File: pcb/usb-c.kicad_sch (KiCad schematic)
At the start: 4 parts, among them J1 USB_C_Receptacle_PowerOnly_6P, J12 Conn_01x02_Pin

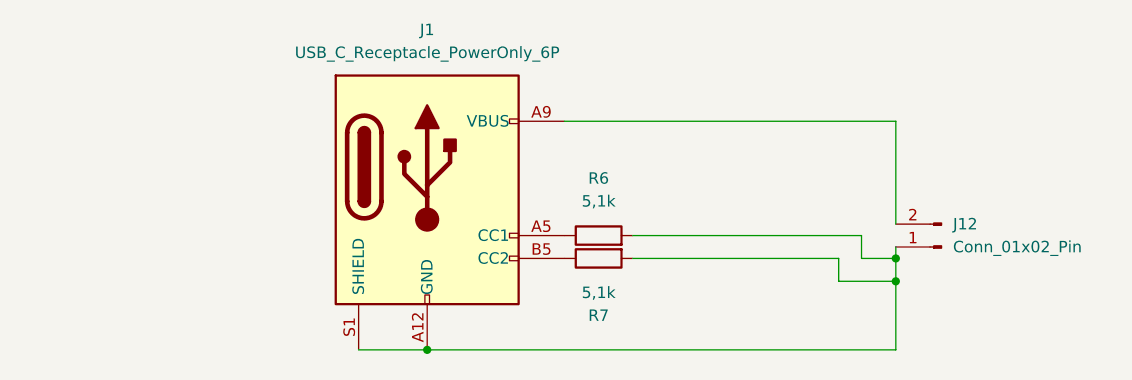
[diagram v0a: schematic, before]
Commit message: Finishing the usb-c module
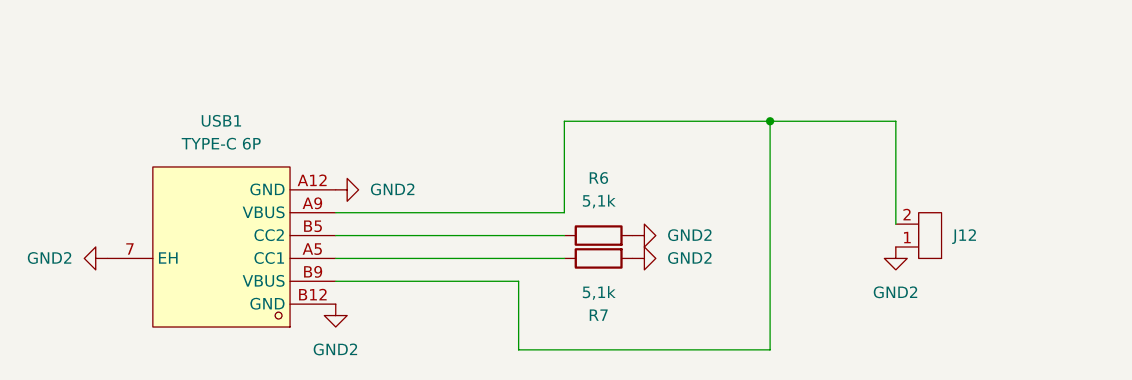
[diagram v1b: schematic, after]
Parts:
- removed J1: USB_C_Receptacle_PowerOnly_6P, Connector_USB:USB_C_Receptacle_GCT_USB4125-xx-x_6P_TopMnt_Horizontal, symbol Connector:USB_C_Receptacle_PowerOnly_6P
- removed J12: Conn_01x02_Pin, Library:copper_pad 2x, symbol Connector:Conn_01x02_Pin
- added J12: (no value), Library:copper_pad 2x, symbol New_Library:copper_pad_2x
- added USB1: TYPE-C 6P, lcsc_import:TYPE-C-SMD_TYPE-C-6P-073, symbol lcsc_import:TYPE-C6P
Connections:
- net GND2: now reaches R6.2, R7.2
- net GND2: now also J12.1, USB1.7 (EH), USB1.A12 (GND), USB1.B12 (GND)
- net at R6.1: now also USB1.B5 (CC2)
- net at R7.1: now also USB1.A5 (CC1)
- new net: J12.2, USB1.A9 (VBUS), USB1.B9 (VBUS)

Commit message: Finishing the carrier board with the new usb-c modul
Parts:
- renumbered R6 to R8, R7 to R9
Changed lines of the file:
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@@
 		(dnp no)
 		(fields_autoplaced yes)
-		(property "Reference" "#PWR037"
+		(property "Reference" "#PWR032"
 			(at 44.45 93.98 0)
 			(hide yes)
@@
 			(project "pcb"
 				(path "/2955ee96-3683-4cf6-bfa3-83b5e4980920/987d3c68-4f18-439b-bf60-3e9251430e23"
-					(reference "#PWR037")
+					(reference "#PWR032")
 					(unit 1)
 				)
@@
 		(dnp no)
 		(fields_autoplaced yes)
-		(property "Reference" "#PWR029"
+		(property "Reference" "#PWR037"
 			(at 138.43 99.06 0)
 			(hide yes)
@@
 			(project "pcb"
 				(path "/2955ee96-3683-4cf6-bfa3-83b5e4980920/987d3c68-4f18-439b-bf60-3e9251430e23"
-					(reference "#PWR029")
+					(reference "#PWR037")
 					(unit 1)
 				)
@@
 		(dnp no)
 		(fields_autoplaced yes)
-		(property "Reference" "#PWR034"
+		(property "Reference" "#PWR035"
 			(at 115.57 91.44 0)
 			(hide yes)
@@
 			(project "pcb"
 				(path "/2955ee96-3683-4cf6-bfa3-83b5e4980920/987d3c68-4f18-439b-bf60-3e9251430e23"
-					(reference "#PWR034")
+					(reference "#PWR035")
 					(unit 1)
 				)
@@
 		(dnp no)
 		(fields_autoplaced yes)
-		(property "Reference" "#PWR036"
+		(property "Reference" "#PWR034"
 			(at 76.2 105.41 0)
 			(hide yes)
@@
 			(project "pcb"
 				(path "/2955ee96-3683-4cf6-bfa3-83b5e4980920/987d3c68-4f18-439b-bf60-3e9251430e23"
-					(reference "#PWR036")
+					(reference "#PWR034")
 					(unit 1)
 				)
@@
 		(dnp no)
 		(fields_autoplaced yes)
-		(property "Reference" "#PWR035"
+		(property "Reference" "#PWR033"
 			(at 82.55 86.36 0)
 			(hide yes)
@@
 			(project "pcb"
 				(path "/2955ee96-3683-4cf6-bfa3-83b5e4980920/987d3c68-4f18-439b-bf60-3e9251430e23"
-					(reference "#PWR035")
+					(reference "#PWR033")
 					(unit 1)
 				)
@@
 		(dnp no)
 		(fields_autoplaced yes)
-		(property "Reference" "#PWR030"
+		(property "Reference" "#PWR036"
 			(at 115.57 93.98 0)
 			(hide yes)
@@
 			(project "pcb"
 				(path "/2955ee96-3683-4cf6-bfa3-83b5e4980920/987d3c68-4f18-439b-bf60-3e9251430e23"
-					(reference "#PWR030")
+					(reference "#PWR036")
 					(unit 1)
 				)
@@
 		(dnp no)
 		(fields_autoplaced yes)
-		(property "Reference" "R6"
+		(property "Reference" "R8"
 			(at 105.41 85.09 90)
 			(show_name no)
@@
 			(project "pcb"
 				(path "/2955ee96-3683-4cf6-bfa3-83b5e4980920/987d3c68-4f18-439b-bf60-3e9251430e23"
-					(reference "R6")
+					(reference "R8")
 					(unit 1)
 				)
@@
 		(in_pos_files yes)
 		(dnp no)
-		(property "Reference" "R7"
+		(property "Reference" "R9"
 			(at 105.41 100.33 90)
 			(show_name no)
@@
 			(project "pcb"
 				(path "/2955ee96-3683-4cf6-bfa3-83b5e4980920/987d3c68-4f18-439b-bf60-3e9251430e23"
-					(reference "R7")
-					(unit 1)
-				)
+					(reference "R9")
+					(unit 1)
+				)
